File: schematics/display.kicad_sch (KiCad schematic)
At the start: 64 parts, among them Q1 S9012, Q10 2N3904, Q11 2N3904, Q12 2N3904, Q13 2N3904, Q14 2N3904, Q15 2N3904, Q16 2N3904, Q17 2N3904, Q2 S9012, Q3 S9012, Q4 S9012, Q5 S9012, Q6 S9012, Q7 S9012, Q8 S9012, Q9 2N3904, U12 74HC138, U13 5161BS, U14 74HC251, U15 5161BS, U16 74HC251, U17 5161BS, U18 5161BS, U19 74HC251, U20 5161BS, U21 5161BS, U22 74HC251, U23 74HC4511, U24 5161BS, U25 5161BS, U26 5161BS

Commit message: 24-12 converter cleanup
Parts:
- removed Q1, Q2, Q3, Q4, Q5, Q6, Q7: S9012, Package_TO_SOT_THT:TO-92_Inline, symbol Transistor_BJT:Q_PNP_EBC
- removed Q10, Q11, Q12, Q13, Q14, Q9: 2N3904, Package_TO_SOT_THT:TO-92_Inline, symbol Transistor_BJT:2N3904
- removed R22, R23, R24, R25, R26, R27, R28: 1K, symbol Device:R
- added Q10, Q11, Q12, Q13, Q14, Q24, Q9: S9012, Package_TO_SOT_THT:TO-92_Inline, symbol Transistor_BJT:Q_PNP_EBC
- added Q18, Q19, Q20, Q21, Q22, Q23: 2N3904, Package_TO_SOT_THT:TO-92_Inline, symbol Transistor_BJT:2N3904
- added R44, R45, R46, R47, R55, R56: 10K, symbol Device:R
- added R57: 1K, symbol Device:R
- R30, R31, R32, R34, R35, R36: value 10K -> 1K
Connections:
- net +3V3: now also Q10.1 (E), Q11.1 (E), Q12.1 (E), Q13.1 (E), Q14.1 (E), Q24.1 (E), Q9.1 (E)
- net VEE: now also Q18.1 (E), Q19.1 (E), Q20.1 (E), Q21.1 (E), Q22.1 (E), Q23.1 (E)
- net at R36.2: now also U12.14 (~{Y1})
- net at U13.6 (B), U15.6 (B), U17.6 (B)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: now also Q18.3 (C)
- net at U13.1 (E), U15.1 (E), U17.1 (E)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: now also Q21.3 (C)
- net at U13.10 (G), U15.10 (G), U17.10 (G)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: now also Q23.3 (C)
- net at U13.2 (D), U15.2 (D), U17.2 (D)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: now also Q20.3 (C)
- net at U21.3 (CA), U21.8 (CA): now also Q10.3 (C)
- net at U13.4 (C), U15.4 (C), U17.4 (C)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: now also Q19.3 (C)
- net at U13.9 (F), U15.9 (F), U17.9 (F)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: now also Q22.3 (C)
- net at R34.2: now also U12.12 (~{Y3})
- net at R32.1: now also Q12.2 (B); no longer U23.9 (e)
- net at R32.2: now also U12.11 (~{Y4})
- net at R37.2: now also U23.14 (g); no longer Q15.2 (B)
- net at R30.2: now also U12.9 (~{Y6})
- net at R29.1: now also Q24.2 (B); no longer Q8.2 (B)
- net at U18.3 (CA), U18.8 (CA): now also Q12.3 (C)
- net at U12.15 (~{Y0}): now also R57.2; no longer R29.2
- net at U20.3 (CA), U20.8 (CA): now also Q11.3 (C)
- net at R31.1: now also Q13.2 (B); no longer U23.15 (f)
- net at R31.2: now also U12.10 (~{Y5})
- net at U17.3 (CA), U17.8 (CA): now also Q13.3 (C)
- net at U12.13 (~{Y2}): now also R35.2
- net at U23.10 (d): now also R46.2; no longer R34.1
- net at U23.11 (c): now also R47.2; no longer R35.1
- net at U23.12 (b): now also R55.2; no longer R36.1
- net at R37.1: now also Q23.2 (B); no longer U23.13 (a)
- net at R30.1: now also Q14.2 (B); no longer U23.14 (g)
- net at U24.3 (CA), U24.8 (CA): now also Q9.3 (C)
- net at U15.3 (CA), U15.8 (CA): now also Q14.3 (C)
- net at U13.3 (CA), U13.8 (CA): now also Q24.3 (C)
- net ~{HHSEL}: no longer names the net of U12.7 (~{Y7})
- net ~{HHSEL}: now also R29.2
- new net: Q19.2 (B), R47.1
- new net: Q18.2 (B), R55.1
- new net: Q10.2 (B), R35.1
- new net: Q8.2 (B), R57.1
- new net: Q20.2 (B), R46.1
- new net: Q22.2 (B), R44.1
- new net: R44.2, U23.15 (f)
- new net: Q21.2 (B), R45.1
- new net: Q11.2 (B), R34.1
- new net: Q15.2 (B), R56.1
- new net: R56.2, U23.13 (a)
- new net: Q9.2 (B), R36.1
- new net: R45.2, U23.9 (e)
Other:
- moved on the sheet: C20, C21, C22, C23, C24, C25, D24, D25, D26, D27, Q16, Q17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

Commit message: added some PCB footprints
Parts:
- C25: renamed from C20; footprint Package_SO:SOIC-8_3.9x4.9mm_P1.27mm -> Capacitor_THT:C_Disc_D5.1mm_W3.2mm_P5.00mm
- C26: renamed from C21; footprint Package_SO:SOIC-8_3.9x4.9mm_P1.27mm -> Capacitor_THT:C_Disc_D5.1mm_W3.2mm_P5.00mm
- C27: renamed from C22; footprint Package_SO:SOIC-8_3.9x4.9mm_P1.27mm -> Capacitor_THT:C_Disc_D5.1mm_W3.2mm_P5.00mm
- C28: renamed from C23; footprint Package_SO:SOIC-8_3.9x4.9mm_P1.27mm -> Capacitor_THT:C_Disc_D5.1mm_W3.2mm_P5.00mm
- C29: renamed from C24; footprint Package_SO:SOIC-8_3.9x4.9mm_P1.27mm -> Capacitor_THT:C_Disc_D5.1mm_W3.2mm_P5.00mm
- C30: renamed from C25; footprint Package_SO:SOIC-8_3.9x4.9mm_P1.27mm -> Capacitor_THT:C_Disc_D5.1mm_W3.2mm_P5.00mm
- D53: renamed from D24; footprint (none) -> LED_THT:LED_D5.0mm
- D54: renamed from D25; footprint (none) -> LED_THT:LED_D5.0mm
- D55: renamed from D26; footprint (none) -> LED_THT:LED_D5.0mm
- D56: renamed from D27; footprint (none) -> LED_THT:LED_D5.0mm
- R29: renamed from R38; footprint (none) -> Resistor_THT:R_Axial_DIN0207_L6.3mm_D2.5mm_P10.16mm_Horizontal
- R30: renamed from R39; footprint (none) -> Resistor_THT:R_Axial_DIN0207_L6.3mm_D2.5mm_P10.16mm_Horizontal
- R31: renamed from R40; footprint (none) -> Resistor_THT:R_Axial_DIN0207_L6.3mm_D2.5mm_P10.16mm_Horizontal
- R32: renamed from R41; footprint (none) -> Resistor_THT:R_Axial_DIN0207_L6.3mm_D2.5mm_P10.16mm_Horizontal
- R33: renamed from R42; footprint (none) -> Resistor_THT:R_Axial_DIN0207_L6.3mm_D2.5mm_P10.16mm_Horizontal
- R34: renamed from R43; footprint (none) -> Resistor_THT:R_Axial_DIN0207_L6.3mm_D2.5mm_P10.16mm_Horizontal
- R35: renamed from R57; footprint (none) -> Resistor_THT:R_Axial_DIN0207_L6.3mm_D2.5mm_P10.16mm_Horizontal
- R36, R46: footprint (none) -> Resistor_THT:R_Axial_DIN0207_L6.3mm_D2.5mm_P10.16mm_Horizontal
- R37: renamed from R35; footprint (none) -> Resistor_THT:R_Axial_DIN0207_L6.3mm_D2.5mm_P10.16mm_Horizontal
- R38: renamed from R34; footprint (none) -> Resistor_THT:R_Axial_DIN0207_L6.3mm_D2.5mm_P10.16mm_Horizontal
- R39: renamed from R32; footprint (none) -> Resistor_THT:R_Axial_DIN0207_L6.3mm_D2.5mm_P10.16mm_Horizontal
- R40: renamed from R31; footprint (none) -> Resistor_THT:R_Axial_DIN0207_L6.3mm_D2.5mm_P10.16mm_Horizontal
- R41: renamed from R30; footprint (none) -> Resistor_THT:R_Axial_DIN0207_L6.3mm_D2.5mm_P10.16mm_Horizontal
- R42: renamed from R29; footprint (none) -> Resistor_THT:R_Axial_DIN0207_L6.3mm_D2.5mm_P10.16mm_Horizontal
- R43: renamed from R56; footprint (none) -> Resistor_THT:R_Axial_DIN0207_L6.3mm_D2.5mm_P10.16mm_Horizontal
- R44: renamed from R55; footprint (none) -> Resistor_THT:R_Axial_DIN0207_L6.3mm_D2.5mm_P10.16mm_Horizontal
- R45: renamed from R47; footprint (none) -> Resistor_THT:R_Axial_DIN0207_L6.3mm_D2.5mm_P10.16mm_Horizontal
- R47: renamed from R45; footprint (none) -> Resistor_THT:R_Axial_DIN0207_L6.3mm_D2.5mm_P10.16mm_Horizontal
- R48: renamed from R44; footprint (none) -> Resistor_THT:R_Axial_DIN0207_L6.3mm_D2.5mm_P10.16mm_Horizontal
- R49: renamed from R37; footprint (none) -> Resistor_THT:R_Axial_DIN0207_L6.3mm_D2.5mm_P10.16mm_Horizontal
- R50: renamed from R33; footprint (none) -> Resistor_THT:R_Axial_DIN0207_L6.3mm_D2.5mm_P10.16mm_Horizontal
- U17: renamed from U16; footprint Package_DIP:DIP-28_W15.24mm -> Package_DIP:DIP-16_W7.62mm
- U18: renamed from U22; footprint Package_DIP:DIP-28_W15.24mm -> Package_DIP:DIP-16_W7.62mm
- U19: renamed from U14; footprint Package_DIP:DIP-28_W15.24mm -> Package_DIP:DIP-16_W7.62mm
- U20: renamed from U19; footprint Package_DIP:DIP-28_W15.24mm -> Package_DIP:DIP-16_W7.62mm
- U21: renamed from U12; footprint Package_TO_SOT_SMD:SOT-23-5 -> Package_DIP:DIP-16_W7.62mm
- U22: renamed from U23; footprint (none) -> Package_DIP:DIP-16_W7.62mm
- renumbered Q16 to Q1, Q24 to Q10, Q15 to Q11, Q18 to Q12, Q19 to Q13, Q20 to Q14, Q21 to Q15, Q22 to Q16, Q23 to Q17, Q17 to Q2, Q8 to Q3, Q9 to Q4, Q10 to Q5, Q11 to Q6, Q12 to Q7, Q13 to Q8, Q14 to Q9, U26 to U16, U25 to U23, U21 to U25, U20 to U26, U18 to U27, U17 to U28, U15 to U29, U13 to U30

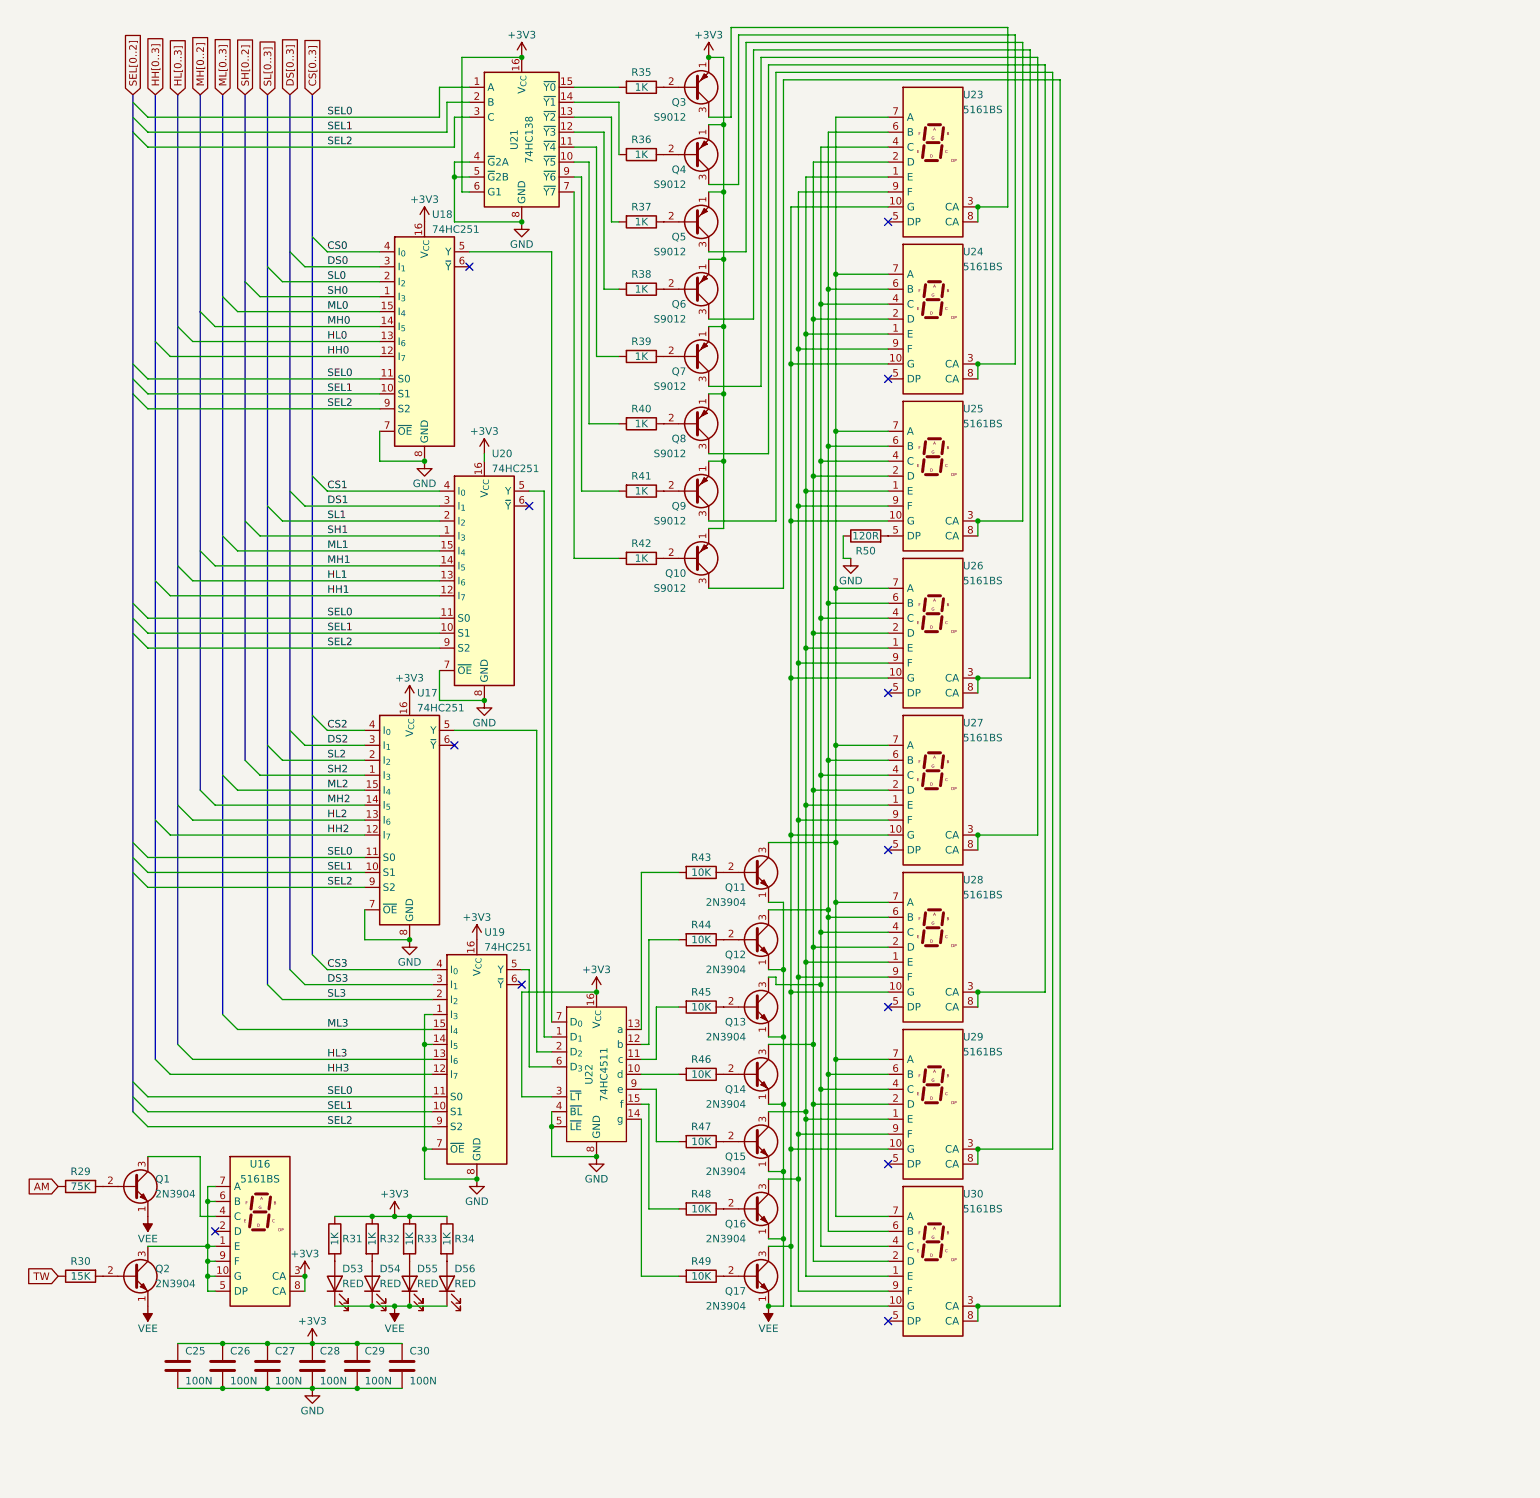
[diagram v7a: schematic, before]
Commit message: switched to PWM for LEDs
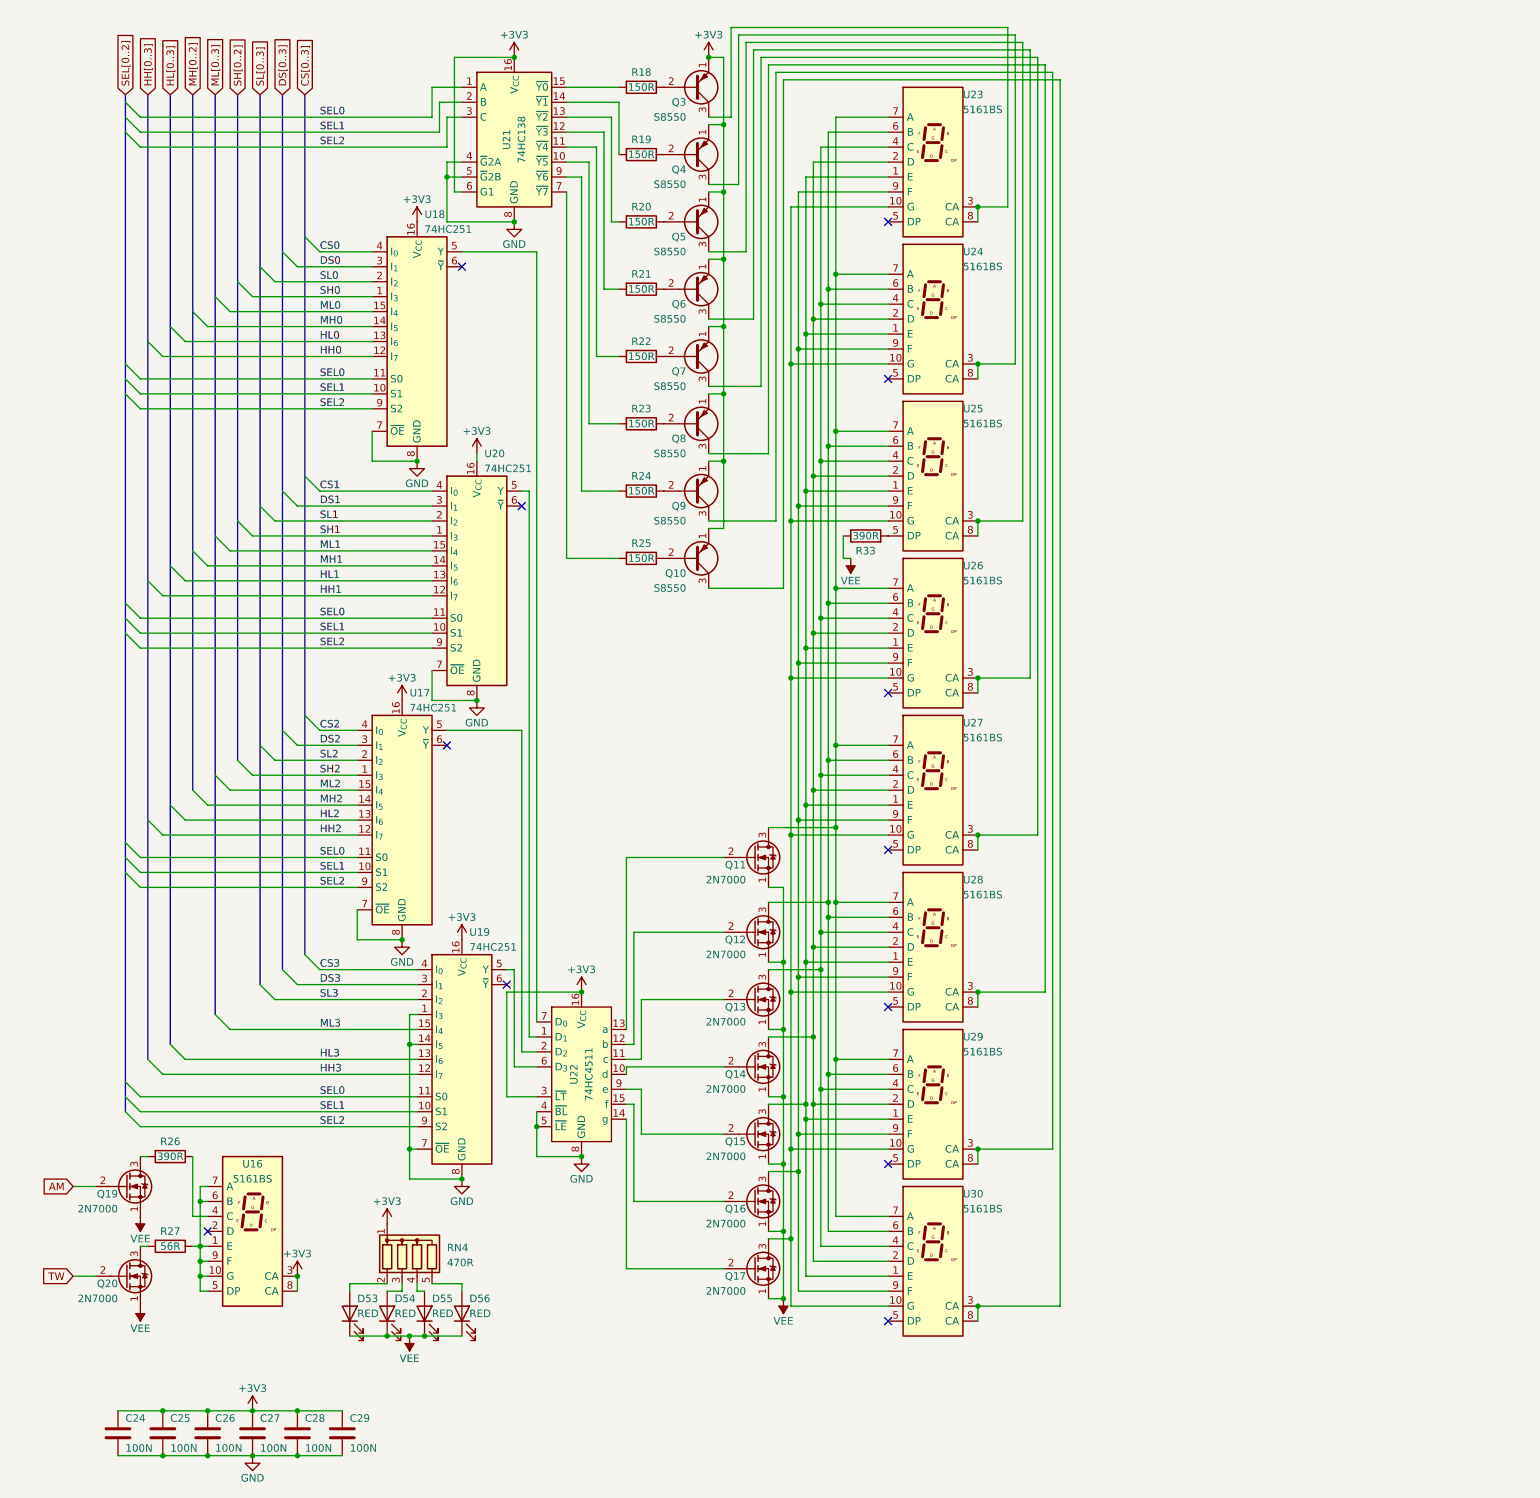
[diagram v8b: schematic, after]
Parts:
- removed Q1, Q11, Q12, Q13, Q14, Q15, Q16, Q17, Q2: 2N3904, Package_TO_SOT_THT:TO-92_Inline, symbol Transistor_BJT:2N3904
- removed R29: 75K, Resistor_THT:R_Axial_DIN0207_L6.3mm_D2.5mm_P10.16mm_Horizontal, symbol Device:R
- removed R30: 15K, Resistor_THT:R_Axial_DIN0207_L6.3mm_D2.5mm_P10.16mm_Horizontal, symbol Device:R
- removed R31, R32, R33, R34: 1K, Resistor_THT:R_Axial_DIN0207_L6.3mm_D2.5mm_P10.16mm_Horizontal, symbol Device:R
- removed R43, R44, R45, R46, R47, R48, R49: 10K, Resistor_THT:R_Axial_DIN0207_L6.3mm_D2.5mm_P10.16mm_Horizontal, symbol Device:R
- added Q11, Q12, Q13, Q14, Q15, Q16, Q17, Q19, Q20: 2N7000, Package_TO_SOT_THT:TO-92_HandSolder, symbol Transistor_FET:2N7000
- added R26: 390R, Resistor_THT:R_Axial_DIN0207_L6.3mm_D2.5mm_P7.62mm_Horizontal, symbol Device:R
- added R27: 56R, Resistor_THT:R_Axial_DIN0207_L6.3mm_D2.5mm_P7.62mm_Horizontal, symbol Device:R
- added RN4: 470R, Resistor_THT:R_Array_SIP5, symbol Device:R_Network04
- Q10, Q3, Q4, Q5, Q6, Q7, Q8, Q9: value S9012 -> S8550; footprint Package_TO_SOT_THT:TO-92_Inline -> Package_TO_SOT_THT:TO-92_HandSolder
- R18: renamed from R35; value 1K -> 150R; footprint Resistor_THT:R_Axial_DIN0207_L6.3mm_D2.5mm_P10.16mm_Horizontal -> Resistor_THT:R_Axial_DIN0207_L6.3mm_D2.5mm_P7.62mm_Horizontal
- R19: renamed from R36; value 1K -> 150R; footprint Resistor_THT:R_Axial_DIN0207_L6.3mm_D2.5mm_P10.16mm_Horizontal -> Resistor_THT:R_Axial_DIN0207_L6.3mm_D2.5mm_P7.62mm_Horizontal
- R20: renamed from R37; value 1K -> 150R; footprint Resistor_THT:R_Axial_DIN0207_L6.3mm_D2.5mm_P10.16mm_Horizontal -> Resistor_THT:R_Axial_DIN0207_L6.3mm_D2.5mm_P7.62mm_Horizontal
- R21: renamed from R38; value 1K -> 150R; footprint Resistor_THT:R_Axial_DIN0207_L6.3mm_D2.5mm_P10.16mm_Horizontal -> Resistor_THT:R_Axial_DIN0207_L6.3mm_D2.5mm_P7.62mm_Horizontal
- R22: renamed from R39; value 1K -> 150R; footprint Resistor_THT:R_Axial_DIN0207_L6.3mm_D2.5mm_P10.16mm_Horizontal -> Resistor_THT:R_Axial_DIN0207_L6.3mm_D2.5mm_P7.62mm_Horizontal
- R23: renamed from R40; value 1K -> 150R; footprint Resistor_THT:R_Axial_DIN0207_L6.3mm_D2.5mm_P10.16mm_Horizontal -> Resistor_THT:R_Axial_DIN0207_L6.3mm_D2.5mm_P7.62mm_Horizontal
- R24: renamed from R41; value 1K -> 150R; footprint Resistor_THT:R_Axial_DIN0207_L6.3mm_D2.5mm_P10.16mm_Horizontal -> Resistor_THT:R_Axial_DIN0207_L6.3mm_D2.5mm_P7.62mm_Horizontal
- R25: renamed from R42; value 1K -> 150R; footprint Resistor_THT:R_Axial_DIN0207_L6.3mm_D2.5mm_P10.16mm_Horizontal -> Resistor_THT:R_Axial_DIN0207_L6.3mm_D2.5mm_P7.62mm_Horizontal
- R33: renamed from R50; value 120R -> 390R; footprint Resistor_THT:R_Axial_DIN0207_L6.3mm_D2.5mm_P10.16mm_Horizontal -> Resistor_THT:R_Axial_DIN0207_L6.3mm_D2.5mm_P7.62mm_Horizontal
- U16, U23, U24, U25, U26, U27, U28, U29, U30: footprint Display_7Segment:KCSC02-105 -> Display_7Segment:7SegmentLED_LTS6760_LTS6780
- renumbered C25 to C24, C26 to C25, C27 to C26, C28 to C27, C29 to C28, C30 to C29
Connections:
- net +3V3: now also RN4.1 (common)
- net AM: now also Q19.2 (G)
- net GND: no longer R33.1
- net TW: now also Q20.2 (G)
- net VEE: now also R33.1, Q11.1 (S), Q12.1 (S), Q13.1 (S), Q14.1 (S), Q15.1 (S), Q16.1 (S), Q17.1 (S), Q19.1 (S), Q20.1 (S)
- net at U16.1 (E), U16.10 (G), U16.5 (DP)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: now also R27.1
- net at U23.1 (E), U24.1 (E), U25.1 (E)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: now also Q15.3 (D)
- net at U23.10 (G), U24.10 (G), U25.10 (G)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: now also Q17.3 (D)
- net at U23.2 (D), U24.2 (D), U25.2 (D)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: now also Q14.3 (D)
- net at U23.4 (C), U24.4 (C), U25.4 (C)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: now also Q13.3 (D)
- net at U23.6 (B), U24.6 (B), U25.6 (B)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: now also Q12.3 (D)
- net at U23.7 (A), U24.7 (A), U25.7 (A)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: now also Q11.3 (D)
- net at U23.9 (F), U24.9 (F), U25.9 (F)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: now also Q16.3 (D)
- net at D55.2 (A): now also RN4.4 (R3)
- net at U22.11 (c): now also Q13.2 (G)
- net at U22.12 (b): now also Q12.2 (G)
- net at D53.2 (A): now also RN4.2 (R1)
- net at U22.10 (d): now also Q14.2 (G)
- net at D56.2 (A): now also RN4.5 (R4)
- net at U22.15 (f): now also Q16.2 (G)
- net at U22.14 (g): now also Q17.2 (G)
- net at U22.13 (a): now also Q11.2 (G)
- net at D54.2 (A): now also RN4.3 (R2)
- net at U22.9 (e): now also Q15.2 (G)
- net at U16.4 (C): now also R26.1
- new net: Q19.3 (D), R26.2
- new net: Q20.3 (D), R27.2
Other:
- moved on the sheet: C24, C25, C26, C27, C28, C29, D53, D54, D55, D56, U16, U17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
